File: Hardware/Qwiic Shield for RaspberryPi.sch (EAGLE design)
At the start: 22 parts, among them J1 Qwiic Right Angle, J10 RASPBERRYPI-40-PIN-GPIO_PTH_N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, J6 Qwiic Right Angle, J7 Qwiic Right Angle, J8 Qwiic Right Angle, U2 3.3V/600mA

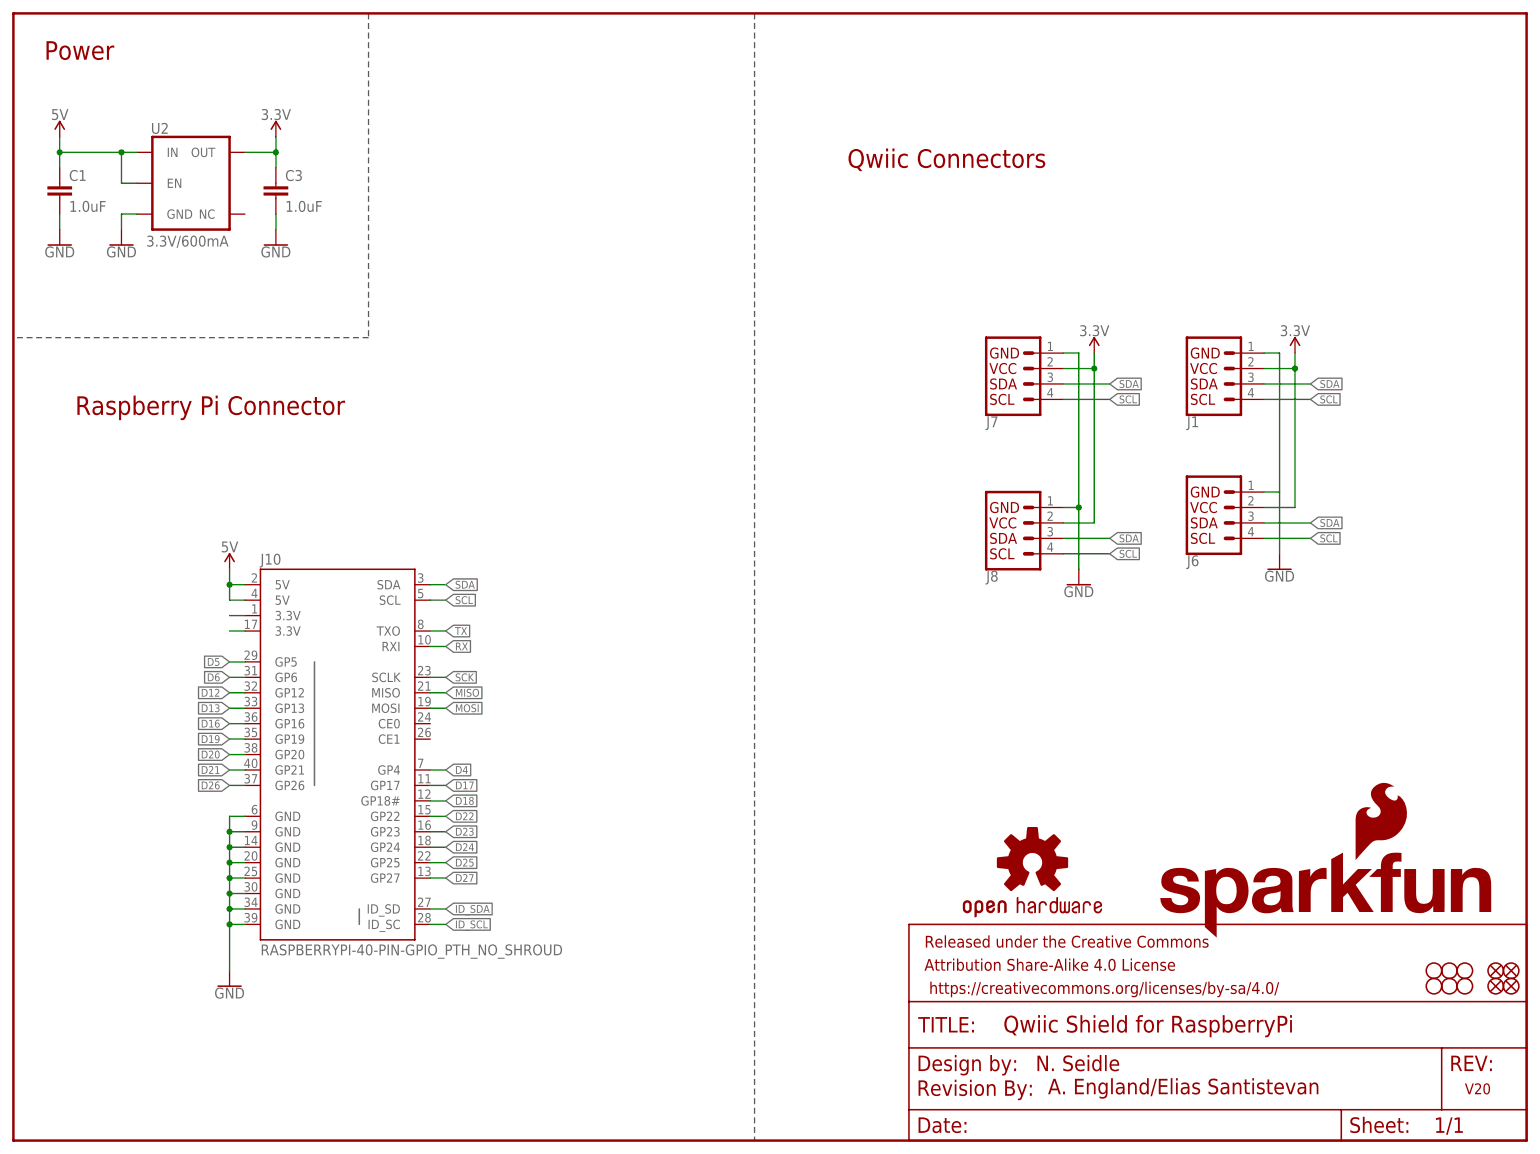
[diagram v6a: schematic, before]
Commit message: Adds I2C pullup resistors
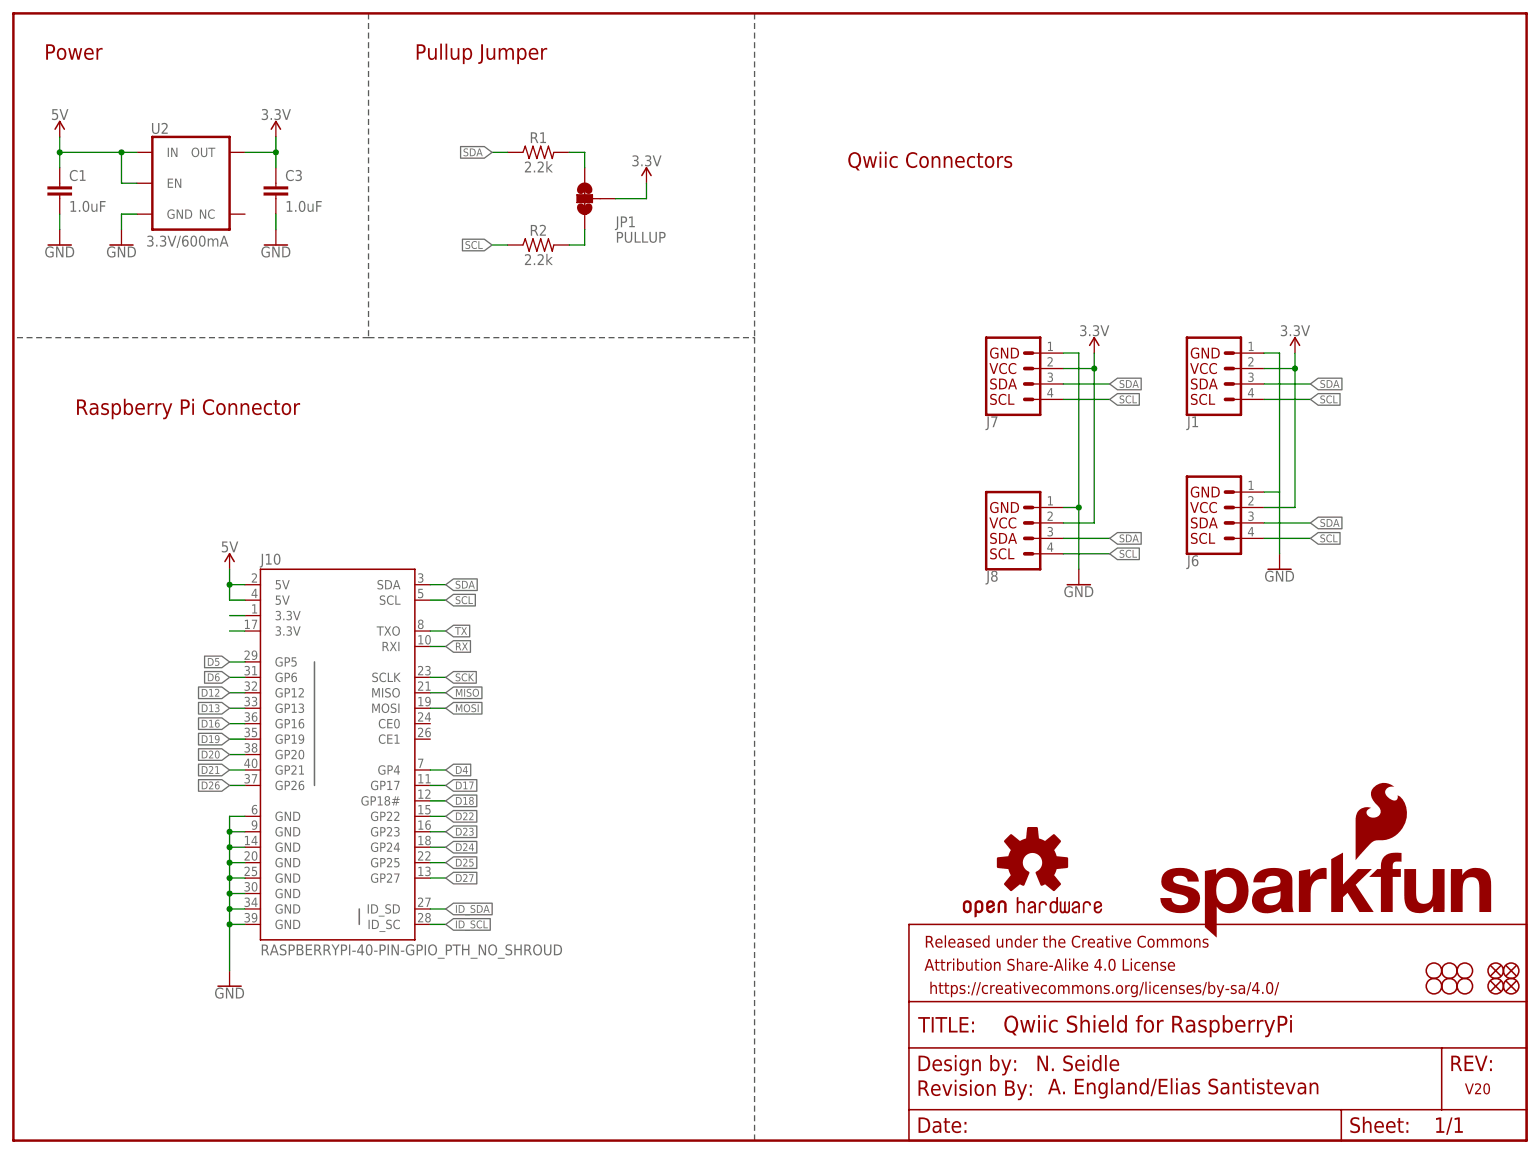
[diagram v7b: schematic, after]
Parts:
- added JP1: PULLUP, SparkFun-Jumpers:JUMPER-SMT_3_2-NC_TRACE_NO-SILK
- added R1, R2: 2.2k, SparkFun-Resistors:2.2KOHM-0603-1/10W-1%
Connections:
- new net N$3: JP1.3, R1.2
- new net N$4: JP1.1, R2.2
- net 3.3V: now also JP1.2
- net SCL: now also R2.1
- net SDA: now also R1.1
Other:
- note added: "Pullup Jumper"
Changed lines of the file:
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@@
 <part name="LOGO1" library="SparkFun-Aesthetics" deviceset="SFE_LOGO_NAME_FLAME" device=".2_INCH"/>
 <part name="LOGO3" library="SparkFun-Aesthetics" deviceset="OSHW-LOGO" device="S" value="OSHW-LOGOS"/>
+<part name="JP1" library="SparkFun-Jumpers" deviceset="JUMPER-SMT_3_2-NC_TRACE" device="_NO-SILK" value="PULLUP"/>
+<part name="SUPPLY1" library="SparkFun-PowerSymbols" deviceset="3.3V" device=""/>
+<part name="R1" library="SparkFun-Resistors" deviceset="2.2KOHM" device="-0603-1/10W-1%" value="2.2k"/>
+<part name="R2" library="SparkFun-Resistors" deviceset="2.2KOHM" device="-0603-1/10W-1%" value="2.2k"/>
 </parts>
 <sheets>
@@
 <plain>
 <text x="168.148" y="11.43" size="2.54" layer="94" font="vector">N. Seidle</text>
-<text x="10.16" y="119.38" size="3.048" layer="94" font="vector" ratio="12">Raspberry Pi Connector</text>
+<text x="10.16" y="119.38" size="2.54" layer="94" font="vector" ratio="12">Raspberry Pi Connector</text>
 <text x="238.76" y="7.62" size="1.778" layer="94" font="vector" ratio="12">V20</text>
-<text x="137.16" y="160.02" size="3.048" layer="94" font="vector" ratio="12">Qwiic Connectors</text>
-<text x="5.08" y="177.8" size="3.048" layer="94" font="vector" ratio="12">Power</text>
+<text x="137.16" y="160.02" size="2.54" layer="94" font="vector" ratio="12">Qwiic Connectors</text>
+<text x="5.08" y="177.8" size="2.54" layer="94" font="vector" ratio="12">Power</text>
 <text x="170.18" y="7.62" size="2.54" layer="94" font="vector">A. England/Elias Santistevan</text>
 <wire x1="58.42" y1="185.42" x2="58.42" y2="132.08" width="0.1524" layer="97" style="shortdash"/>
 <wire x1="58.42" y1="132.08" x2="0" y2="132.08" width="0.1524" layer="97" style="shortdash"/>
-<wire x1="121.92" y1="185.42" x2="121.92" y2="0" width="0.2032" layer="97" style="shortdash"/>
+<wire x1="121.92" y1="185.42" x2="121.92" y2="132.08" width="0.2032" layer="97" style="shortdash"/>
+<wire x1="121.92" y1="132.08" x2="121.92" y2="0" width="0.2032" layer="97" style="shortdash"/>
+<wire x1="58.42" y1="132.08" x2="121.92" y2="132.08" width="0.2032" layer="97" style="shortdash"/>
+<text x="66.04" y="177.8" size="2.54" layer="94" font="vector" ratio="12">Pullup Jumper</text>
 </plain>
 <instances>
@@
 <instance part="LOGO1" gate="G$1" x="187.96" y="33.02" smashed="yes"/>
 <instance part="LOGO3" gate="G$1" x="167.64" y="45.72" smashed="yes"/>
+<instance part="JP1" gate="G$1" x="93.98" y="154.94" smashed="yes" rot="R180">
+<attribute name="NAME" x="99.06" y="150.241" size="1.778" layer="95" font="vector"/>
+<attribute name="VALUE" x="99.06" y="149.479" size="1.778" layer="96" font="vector" align="top-left"/>
+</instance>
+<instance part="SUPPLY1" gate="G$1" x="104.14" y="157.48" smashed="yes">
+<attribute name="VALUE" x="104.14" y="160.274" size="1.778" layer="96" align="bottom-center"/>
+</instance>
+<instance part="R1" gate="G$1" x="86.36" y="162.56" smashed="yes">
+<attribute name="NAME" x="86.36" y="164.084" size="1.778" layer="95" font="vector" align="bottom-center"/>
+<attribute name="VALUE" x="86.36" y="161.036" size="1.778" layer="96" font="vector" align="top-center"/>
+</instance>
+<instance part="R2" gate="G$1" x="86.36" y="147.32" smashed="yes">
+<attribute name="NAME" x="86.36" y="148.844" size="1.778" layer="95" font="vector" align="bottom-center"/>
+<attribute name="VALUE" x="86.36" y="145.796" size="1.778" layer="96" font="vector" align="top-center"/>
+</instance>
 </instances>
 <busses>
@@
 <junction x="177.8" y="127"/>
 </segment>
+<segment>
+<pinref part="JP1" gate="G$1" pin="2"/>
+<wire x1="99.06" y1="154.94" x2="104.14" y2="154.94" width="0.1524" layer="91"/>
+<pinref part="SUPPLY1" gate="G$1" pin="3.3V"/>
+<wire x1="104.14" y1="154.94" x2="104.14" y2="157.48" width="0.1524" layer="91"/>
+</segment>
 </net>
 <net name="SDA" class="0">
@@
 <label x="71.12" y="91.44" size="1.27" layer="95" font="vector" xref="yes"/>
 </segment>
+<segment>
+<pinref part="R1" gate="G$1" pin="1"/>
+<wire x1="81.28" y1="162.56" x2="78.74" y2="162.56" width="0.1524" layer="91"/>
+<label x="78.74" y="162.56" size="1.27" layer="95" rot="R180" xref="yes"/>
+</segment>
 </net>
 <net name="SCL" class="0">
@@
 <wire x1="68.58" y1="88.9" x2="71.12" y2="88.9" width="0.1524" layer="91"/>
 <label x="71.12" y="88.9" size="1.27" layer="95" font="vector" xref="yes"/>
+</segment>
+<segment>
+<pinref part="R2" gate="G$1" pin="1"/>
+<wire x1="81.28" y1="147.32" x2="78.74" y2="147.32" width="0.1524" layer="91"/>
+<label x="78.74" y="147.32" size="1.27" layer="95" rot="R180" xref="yes"/>
 </segment>
 </net>
@@
 </segment>
 </net>
+<net name="N$3" class="0">
+<segment>
+<pinref part="JP1" gate="G$1" pin="3"/>
+<wire x1="93.98" y1="160.02" x2="93.98" y2="162.56" width="0.1524" layer="91"/>
+<pinref part="R1" gate="G$1" pin="2"/>
+<wire x1="93.98" y1="162.56" x2="91.44" y2="162.56" width="0.1524" layer="91"/>
+</segment>
+</net>
+<net name="N$4" class="0">
+<segment>
+<pinref part="JP1" gate="G$1" pin="1"/>
+<wire x1="93.98" y1="149.86" x2="93.98" y2="147.32" width="0.1524" layer="91"/>
+<pinref part="R2" gate="G$1" pin="2"/>
+<wire x1="93.98" y1="147.32" x2="91.44" y2="147.32" width="0.1524" layer="91"/>
+</segment>
+</net>
